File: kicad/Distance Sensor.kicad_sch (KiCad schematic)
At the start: 3 parts, among them J1 Conn_01x03, U1 ESP32 C3 Super Mini, U2 VL53LDK

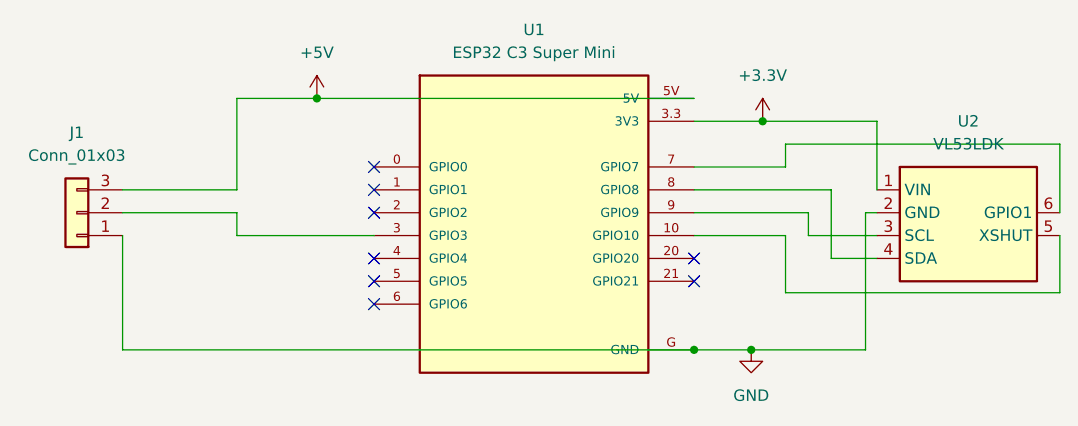
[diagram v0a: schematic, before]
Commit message: Improve footprints
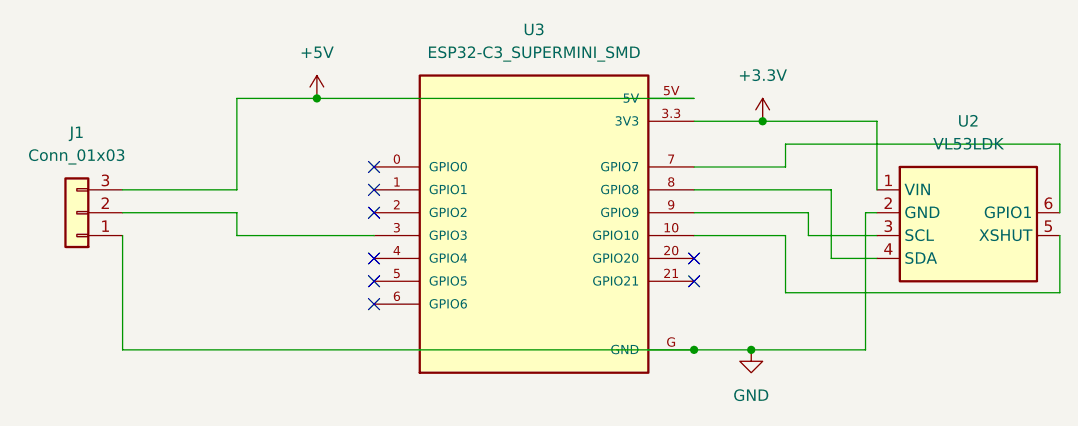
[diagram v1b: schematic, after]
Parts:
- removed U1: ESP32 C3 Super Mini, Distance Sensor:ESP32-C3 Super Mini, symbol ESP32-C3_SUPERMINI:ESP32 C3 Super Mini
- added U3: ESP32-C3_SUPERMINI_SMD, Distance Sensor:MODULE_ESP32-C3_SUPERMINI, symbol ESP32-C3_SUPERMINI_SMD:ESP32-C3_SUPERMINI_SMD
- U2: symbol ESP32-C3_SUPERMINI:VL53LDK -> VL53LDK:VL53LDK
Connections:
- net +3.3V: now also U3.3.3 (3V3)
- net +5V: now also U3.5V
- net GND: now also U3.G (GND)
- net at U2.3 (SCL): now also U3.9 (GPIO9)
- net at U2.4 (SDA): now also U3.8 (GPIO8)
- net at U2.5 (XSHUT): now also U3.10 (GPIO10)
- net at U2.6 (GPIO1): now also U3.7 (GPIO7)
- net at J1.2 (Pin_2): now also U3.3 (GPIO3)
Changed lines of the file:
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@@
+	)
+	(symbol
+		(lib_id "ESP32-C3_SUPERMINI_SMD:ESP32-C3_SUPERMINI_SMD")
+		(at 137.16 92.71 0)
+		(unit 1)
+		(exclude_from_sim no)
+		(in_bom yes)
+		(on_board yes)
+		(dnp no)
+		(fields_autoplaced yes)
+		(property "Reference" "U3"
+			(at 137.16 72.39 0)
+			(effects
+				(font
+					(size 1.27 1.27)
+				)
+			)
+		)
+		(property "Value" "ESP32-C3_SUPERMINI_SMD"
+			(at 137.16 74.93 0)
+			(effects
+				(font
+					(size 1.27 1.27)
+				)
+			)
+		)
+		(property "Footprint" "Distance Sensor:MODULE_ESP32-C3_SUPERMINI"
+			(at 137.16 92.71 0)
+			(effects
+				(font
+					(size 1.27 1.27)
+				)
+				(justify bottom)
+				(hide yes)
+			)
+		)
+		(property "Datasheet" ""
+			(at 137.16 92.71 0)
+			(effects
+				(font
+					(size 1.27 1.27)
+				)
+				(hide yes)
+			)
+		)
+		(property "Description" ""
+			(at 137.16 92.71 0)
+			(effects
+				(font
+					(size 1.27 1.27)
+				)
+				(hide yes)
+			)
+		)
+		(property "MF" "Espressif Systems"
+			(at 137.16 92.71 0)
+			(effects
+				(font
+					(size 1.27 1.27)
+				)
+				(justify bottom)
+				(hide yes)
+			)
+		)
+		(property "MAXIMUM_PACKAGE_HEIGHT" "4.2mm"
+			(at 137.16 92.71 0)
+			(effects
+				(font
+					(size 1.27 1.27)
+				)
+				(justify bottom)
+				(hide yes)
+			)
+		)
+		(property "Package" "None"
+			(at 137.16 92.71 0)
+			(effects
+				(font
+					(size 1.27 1.27)
+				)
+				(justify bottom)
+				(hide yes)
+			)
+		)
+		(property "Price" "None"
+			(at 137.16 92.71 0)
+			(effects
+				(font
+					(size 1.27 1.27)
+				)
+				(justify bottom)
+				(hide yes)
+			)
+		)
+		(property "Check_prices" "https://www.snapeda.com/parts/ESP32-C3%20SuperMini_SMD/Espressif+Systems/view-part/?ref=eda"
+			(at 137.16 92.71 0)
+			(effects
+				(font
+					(size 1.27 1.27)
+				)
+				(justify bottom)
+				(hide yes)
+			)
+		)
+		(property "STANDARD" "Manufacturer Recommendations"
+			(at 137.16 92.71 0)
+			(effects
+				(font
+					(size 1.27 1.27)
+				)
+				(justify bottom)
+				(hide yes)
+			)
+		)
+		(property "PARTREV" ""
+			(at 137.16 92.71 0)
+			(effects
+				(font
+					(size 1.27 1.27)
+				)
+				(justify bottom)
+				(hide yes)
+			)
+		)
+		(property "SnapEDA_Link" "https://www.snapeda.com/parts/ESP32-C3%20SuperMini_SMD/Espressif+Systems/view-part/?ref=snap"
+			(at 137.16 92.71 0)
+			(effects
+				(font
+					(size 1.27 1.27)
+				)
+				(justify bottom)
+				(hide yes)
+			)
+		)
+		(property "MP" "ESP32-C3 SuperMini_SMD"
+			(at 137.16 92.71 0)
+			(effects
+				(font
+					(size 1.27 1.27)
+				)
+				(justify bottom)
+				(hide yes)
+			)
+		)
+		(property "Description_1" "Super tiny ESP32-C3 board"
+			(at 137.16 92.71 0)
+			(effects
+				(font
+					(size 1.27 1.27)
+				)
+				(justify bottom)
+				(hide yes)
+			)
+		)
+		(property "Availability" "Not in stock"
+			(at 137.16 92.71 0)
+			(effects
+				(font
+					(size 1.27 1.27)
+				)
+				(justify bottom)
+				(hide yes)
+			)
+		)
+		(property "MANUFACTURER" "Espressif"
+			(at 137.16 92.71 0)
+			(effects
+				(font
+					(size 1.27 1.27)
+				)
+				(justify bottom)
+				(hide yes)
+			)
+		)
+		(pin "10"
+		)
+		(pin "5V"
+		)
+		(pin "21"
+		)
+		(pin "G"
+		)
+		(pin "5"
+		)
+		(pin "3"
+		)
+		(pin "1"
+		)
+		(pin "0"
+		)
+		(pin "2"
+		)
+		(pin "4"
+		)
+		(pin "6"
+		)
+		(pin "7"
+		)
+		(pin "20"
+		)
+		(pin "3.3"
+		)
+		(pin "8"
+		)
+		(pin "9"
+		)
+		(instances
+			(project ""
+				(path "/b1c6768b-077d-48e9-a05f-8422c10a38ff"
+					(reference "U3")
+					(unit 1)
+				)
+			)
+		)
 	)
 	(symbol
@@
 	)
 	(symbol
-		(lib_id "ESP32-C3_SUPERMINI:VL53LDK")
+		(lib_id "VL53LDK:VL53LDK")
 		(at 185.42 92.71 0)
 		(unit 1)
@@
 					(unit 1)
 				)
-			)
-		)
-	)
-	(symbol
-		(lib_id "ESP32-C3_SUPERMINI:ESP32 C3 Super Mini")
-		(at 137.16 92.71 0)
-		(unit 1)
-		(exclude_from_sim no)
-		(in_bom yes)
-		(on_board yes)
-		(dnp no)
-		(fields_autoplaced yes)
-		(property "Reference" "U1"
-			(at 137.16 72.39 0)
-			(effects
-				(font
-					(size 1.27 1.27)
-				)
-			)
-		)
-		(property "Value" "ESP32 C3 Super Mini"
-			(at 137.16 74.93 0)
-			(effects
-				(font
-					(size 1.27 1.27)
-				)
-			)
-		)
-		(property "Footprint" "Distance Sensor:ESP32-C3 Super Mini"
-			(at 137.16 68.58 0)
-			(effects
-				(font
-					(size 1.27 1.27)
-				)
-				(justify bottom)
-				(hide yes)
-			)
-		)
-		(property "Datasheet" ""
-			(at 137.16 92.71 0)
-			(effects
-				(font
-					(size 1.27 1.27)
-				)
-				(hide yes)
-			)
-		)
-		(property "Description" "Super tiny ESP32-C3 board"
-			(at 137.16 73.66 0)
-			(effects
-				(font
-					(size 1.27 1.27)
-				)
-				(justify bottom)
-				(hide yes)
-			)
-		)
-		(property "MF" ""
-			(at 135.89 100.33 0)
-			(effects
-				(font
-					(size 1.27 1.27)
-				)
-				(justify bottom)
-				(hide yes)
-			)
-		)
-		(property "MAXIMUM_PACKAGE_HEIGHT" ""
-			(at 134.62 95.25 0)
-			(effects
-				(font
-					(size 1.27 1.27)
-				)
-				(justify bottom)
-				(hide yes)
-			)
-		)
-		(property "Package" ""
-			(at 135.89 90.17 0)
-			(effects
-				(font
-					(size 1.27 1.27)
-				)
-				(justify bottom)
-				(hide yes)
-			)
-		)
-		(property "Price" ""
-			(at 135.89 83.82 0)
-			(effects
-				(font
-					(size 1.27 1.27)
-				)
-				(justify bottom)
-				(hide yes)
-			)
-		)
-		(property "Check_prices" ""
-			(at 133.35 106.68 0)
-			(do_not_autoplace yes)
-			(effects
-				(font
-					(size 1.27 1.27)
-				)
-				(justify bottom)
-				(hide yes)
-			)
-		)
-		(property "STANDARD" ""
-			(at 135.89 95.25 0)
-			(effects
-				(font
-					(size 1.27 1.27)
-				)
-				(justify bottom)
-				(hide yes)
-			)
-		)
-		(property "PARTREV" ""
-			(at 137.16 92.71 0)
-			(effects
-				(font
-					(size 1.27 1.27)
-				)
-				(justify bottom)
-				(hide yes)
-			)
-		)
-		(property "SnapEDA_Link" ""
-			(at 135.89 72.39 0)
-			(do_not_autoplace yes)
-			(effects
-				(font
-					(size 1.27 1.27)
-				)
-				(justify bottom)
-				(hide yes)
-			)
-		)
-		(property "MP" "ESP32-C3 SuperMini"
-			(at 137.16 72.39 0)
-			(effects
-				(font
-					(size 1.27 1.27)
-				)
-				(justify bottom)
-				(hide yes)
-			)
-		)
-		(property "Availability" ""
-			(at 135.89 100.33 0)
-			(effects
-				(font
-					(size 1.27 1.27)
-				)
-				(justify bottom)
-				(hide yes)
-			)
-		)
-		(property "MANUFACTURER" ""
-			(at 135.89 86.36 0)
-			(effects
-				(font
-					(size 1.27 1.27)
-				)
-				(justify bottom)
-				(hide yes)
-			)
-		)
-		(pin "1"
-		)
-		(pin "0"
-		)
-		(pin "10"
-		)
-		(pin "20"
-		)
-		(pin "21"
-		)
-		(pin "7"
-		)
-		(pin "5V"
-		)
-		(pin "4"
-		)
-		(pin "8"
-		)
-		(pin "9"
-		)
-		(pin "G"
-		)
-		(pin "5"
-		)
-		(pin "2"
-		)
-		(pin "3"
-		)
-		(pin "3.3"
-		)
-		(pin "6"
-		)
-		(instances
-			(project ""
-				(path "/b1c6768b-077d-48e9-a05f-8422c10a38ff"
-					(reference "U1")
-					(unit 1)
-				)
